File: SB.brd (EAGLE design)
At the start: 78 x 34 mm, 47 parts, among them IC1 ATMEGA32U4NT-TQFP, IC2 HX711-SOP16L, J1 RJ10-WURTH, J2 AUDIO-JACK-PJ321, J3 USB-C-16P-16P, K1 HE721C-DIP, Q1 2N7002, Q2 2N3906, SW1 SWITCH-SPDT-4TABSSMT, SW2 SWITCH-SPDT-4TABSSMT, SW3 RESET, SW4 Trigger Level

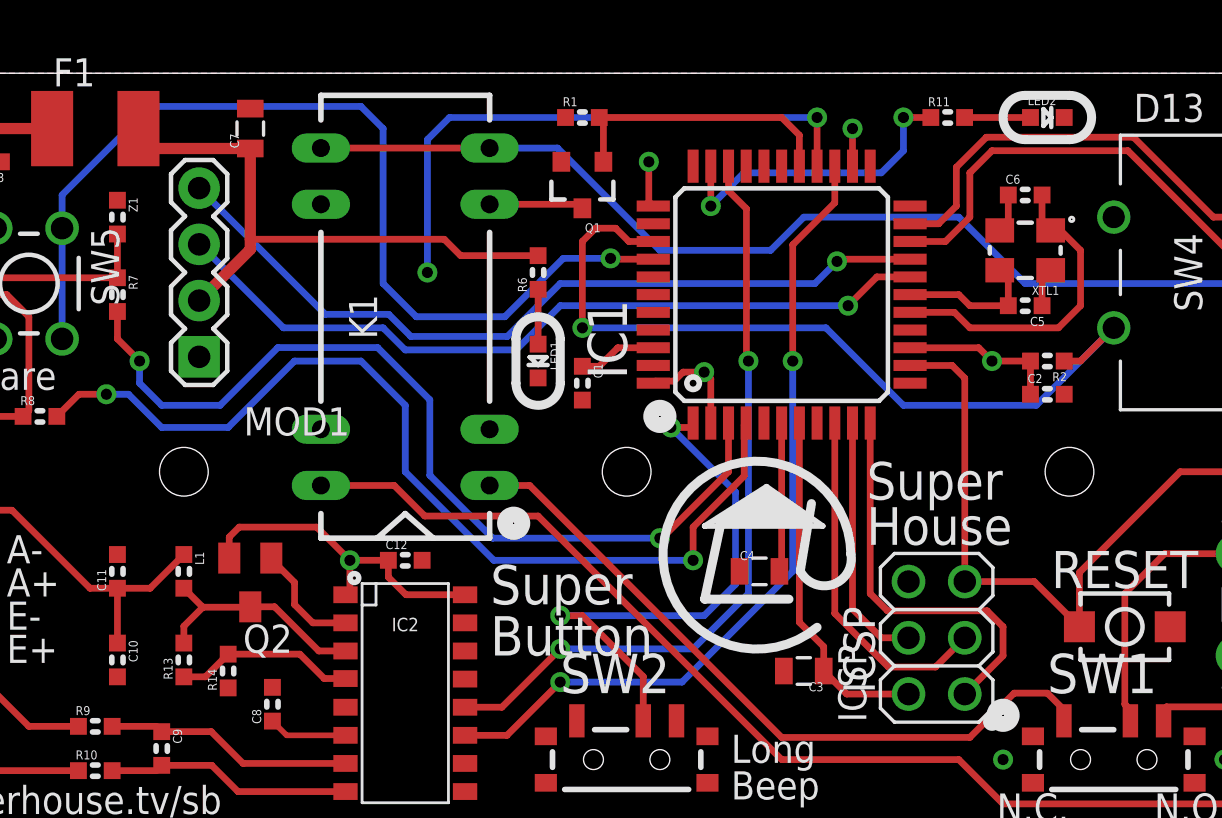
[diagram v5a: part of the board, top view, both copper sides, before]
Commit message: Still for v3.0 release: updated design rules and improved clearances
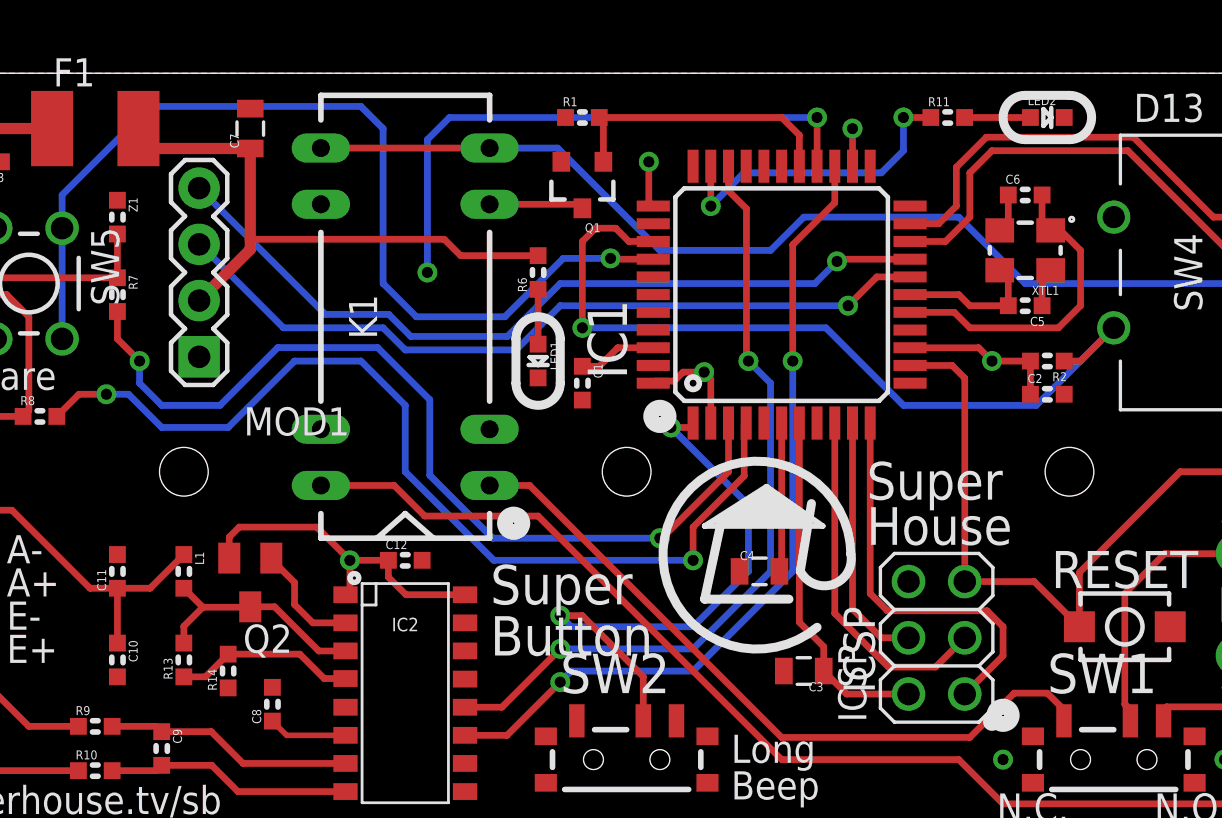
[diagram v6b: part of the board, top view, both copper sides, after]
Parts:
- SW5: value (none) -> Tare
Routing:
- net D7_AIN0: track 24.8 -> 25.7 mm
- net D5: track 34.6 -> 35.4 mm
- net 5V: track 78.7 -> 78.1 mm
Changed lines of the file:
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@@
 <setting verticaltext="up"/>
 </settings>
-<grid distance="1" unitdist="mm" unit="mm" style="lines" multiple="1" display="yes" altdistance="0.005" altunitdist="inch" altunit="inch"/>
+<grid distance="0.5" unitdist="mm" unit="mm" style="lines" multiple="1" display="yes" altdistance="0.005" altunitdist="inch" altunit="inch"/>
 <layers>
 <layer number="1" name="Top" color="12" fill="1" visible="yes" active="yes"/>
@@
 <attribute name="VALUE" x="36" y="-2" size="1.778" layer="27"/>
 </element>
-<element name="SW5" library="SuperHouse-Switches" library_urn="urn:adsk.eagle:library:11744182" package="TACTILE-PTH-4.5MM" package3d_urn="urn:adsk.eagle:package:7066371/2" value="" x="12" y="24.5" locked="yes" smashed="yes" rot="R270">
+<element name="SW5" library="SuperHouse-Switches" library_urn="urn:adsk.eagle:library:11744182" package="TACTILE-PTH-4.5MM" package3d_urn="urn:adsk.eagle:package:7066371/2" value="Tare" x="12" y="24.5" locked="yes" smashed="yes" rot="R270">
 <attribute name="NAME" x="14.81" y="27.04" locked="yes" size="1.27" layer="25" ratio="10" rot="R270"/>
 </element>
@@
 <wire x1="40" y1="30" x2="40" y2="28.2" width="0.3048" layer="1"/>
 <wire x1="40" y1="28.2" x2="40.2" y2="28" width="0.3048" layer="1"/>
-<wire x1="49.2" y1="31.5" x2="49.2" y2="31.3" width="0.3048" layer="1"/>
-<wire x1="49.2" y1="31.3" x2="49.2" y2="29.8" width="0.3048" layer="1"/>
+<wire x1="49.2" y1="31.5" x2="49.2" y2="29.8" width="0.3048" layer="1"/>
 <contactref element="MOD1" pad="VCC"/>
 <contactref element="K1" pad="2"/>
@@
 <wire x1="42.8" y1="20.2" x2="42.5" y2="20.5" width="0.3048" layer="1"/>
 <contactref element="C7" pad="1"/>
-<wire x1="17" y1="32" x2="16.95" y2="31.95" width="0.508" layer="1"/>
-<wire x1="16.95" y1="31.95" x2="16.95" y2="31.5" width="0.508" layer="1"/>
 <contactref element="R2" pad="2"/>
 <wire x1="57.238" y1="21" x2="55.5" y2="21" width="0.3048" layer="1"/>
@@
 <wire x1="53.7" y1="20.8" x2="51.8" y2="20.8" width="0.3048" layer="1"/>
 <wire x1="54.27" y1="20.23" x2="53.7" y2="20.8" width="0.3048" layer="1"/>
-<wire x1="59.45" y1="9" x2="59.738" y2="9" width="0.3048" layer="1"/>
 <wire x1="59.45" y1="9" x2="57.41" y2="11.04" width="0.3048" layer="1"/>
 <wire x1="57.41" y1="11.04" x2="54.27" y2="11.04" width="0.3048" layer="1"/>
@@
 <wire x1="18" y1="19" x2="17" y2="20" width="0.3048" layer="16"/>
 <wire x1="17" y1="20" x2="17" y2="21" width="0.3048" layer="16"/>
-<wire x1="43.6" y1="16" x2="40.6" y2="13" width="0.3048" layer="1"/>
+<wire x1="43.6" y1="16" x2="43.3" y2="15.7" width="0.3048" layer="1"/>
+<wire x1="43.3" y1="15.7" x2="40.6" y2="13" width="0.3048" layer="1"/>
 <wire x1="40.6" y1="13" x2="40.5" y2="13" width="0.3048" layer="1"/>
 </signal>
@@
 <wire x1="44.4104" y1="27.87710625" x2="44.4104" y2="21.0896" width="0.3048" layer="1"/>
 <via x="44.5" y="21" extent="1-16" drill="0.5"/>
-<wire x1="44.5" y1="21" x2="44.5" y2="10.5" width="0.3048" layer="16"/>
-<wire x1="44.5" y1="10.5" x2="42" y2="8" width="0.3048" layer="16"/>
+<wire x1="44.5" y1="21" x2="45.5" y2="20" width="0.3048" layer="16"/>
+<wire x1="45.5" y1="20" x2="45.5" y2="11.5" width="0.3048" layer="16"/>
+<wire x1="45.5" y1="11.5" x2="42" y2="8" width="0.3048" layer="16"/>
 <wire x1="42" y1="8" x2="36" y2="8" width="0.3048" layer="16"/>
 <contactref element="IC2" pad="12"/>
@@
 <wire x1="41.8" y1="18" x2="41" y2="18" width="0.3048" layer="1"/>
 <via x="41" y="18" extent="1-16" drill="0.5"/>
-<wire x1="41" y1="18" x2="43.9158" y2="15.0842" width="0.3048" layer="16"/>
-<wire x1="43.9158" y1="10.9158" x2="42.5" y2="9.5" width="0.3048" layer="16"/>
-<wire x1="43.9158" y1="15.0842" x2="43.9158" y2="10.9158" width="0.3048" layer="16"/>
-<wire x1="42.5" y1="9.5" x2="36" y2="9.5" width="0.3048" layer="16"/>
+<wire x1="42" y1="9" x2="36.5" y2="9" width="0.3048" layer="16"/>
+<wire x1="36.5" y1="9" x2="36" y2="9.5" width="0.3048" layer="16"/>
+<wire x1="41" y1="18" x2="44.5" y2="14.5" width="0.3048" layer="16"/>
+<wire x1="44.5" y1="14.5" x2="44.5" y2="11.5" width="0.3048" layer="16"/>
+<wire x1="44.5" y1="11.5" x2="42" y2="9" width="0.3048" layer="16"/>
 </signal>
 <signal name="D11">
@@
 <wire x1="48.4" y1="28.15" x2="46.5" y2="26.25" width="0.3048" layer="1"/>
 <wire x1="46.5" y1="21" x2="46.5" y2="11.5" width="0.3048" layer="16"/>
-<wire x1="46.5" y1="11.5" x2="41.5" y2="6.5" width="0.3048" layer="16"/>
+<wire x1="46.5" y1="11.5" x2="42" y2="7" width="0.3048" layer="16"/>
 <contactref element="IC2" pad="11"/>
-<wire x1="41.5" y1="6.5" x2="36" y2="6.5" width="0.3048" layer="16"/>
+<wire x1="42" y1="7" x2="36.5" y2="7" width="0.3048" layer="16"/>
+<wire x1="36.5" y1="7" x2="36" y2="6.5" width="0.3048" layer="16"/>
 <via x="36" y="6.5" extent="1-16" drill="0.5"/>
 <wire x1="36" y1="6.5" x2="33.595" y2="4.095" width="0.3048" layer="1"/>
